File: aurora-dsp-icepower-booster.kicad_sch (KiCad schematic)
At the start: 264 parts, among them J1 24V DC, J10 XLR3_OUT, J11 XLR3_OUT, J12 XLR3_OUT, J13 XLR3_OUT, J14 XLR3_OUT, J2 REMOTE 3.5mm, J3 XLR_IN_1, J4 XLR_IN_2, J5 XLR_IN_3, J6 XLR_IN_4, J7 XLR_IN_5, J8 XLR_IN_6, J9 XLR3_OUT, Q1 BSS138, Q2 BSS138, Q3 BSS138, Q4 BSS138, Q5 BSS138, Q6 BSS138, Q7 BSS138, SW1 ALWAYS/REMOTE, SW2 Gain CH1, SW3 Gain CH2, SW4 Gain CH3, SW5 Gain CH4, SW6 Gain CH5, SW7 Gain CH6, U1 TEL5-2422, U10 LM4562, U11 LM4562, U12 LM4562, U13 LM4562, U14 ADP7118ARDZ-11, U15 ADP7182AUJZ-11, U2 LM4562, U3 LM4562, U4 LM4562, U5 LM4562, U6 LM4562, U7 LM4562, U8 LM4562, U9 LM4562

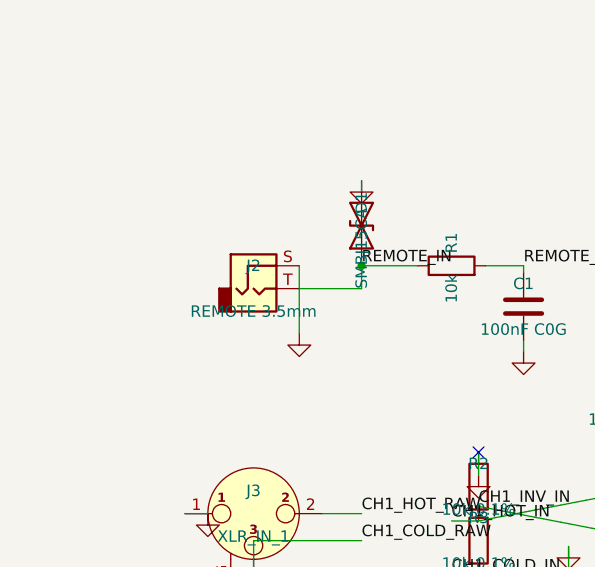
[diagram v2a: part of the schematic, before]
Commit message: feat: Replace J2 Lumberg with KH-PJ-320EA-5P-SMT, add J15 passthrough
- Replaced J2 (Lumberg 1503_02 AudioJack2) with KH-PJ-320EA-5P-SMT (LCSC C5123132)
- Added J15 as identical passthrough jack at (19, 5.08), left of J2 (30.47, 5.08)
- Created custom footprint + symbol with 3D models
- Schematic: J2+J15 Tip→/REMOTE_IN, Sleeve→GND, unused pins→no_connect
- PCB: REMOTE_IN traces routed around J2 Pad5 to avoid short
- DRC: 0 shorts, 0 real unconnected (27 zone fill, 56 warnings)
- ERC: 0 errors, 1059 warnings (baseline)
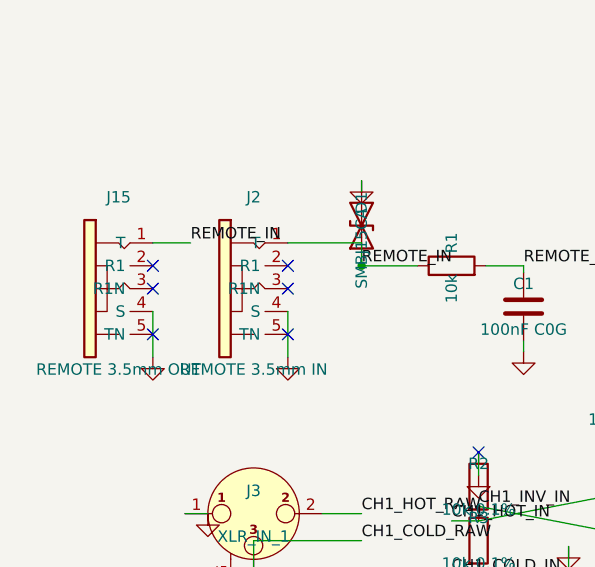
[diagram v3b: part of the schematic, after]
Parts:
- removed J2: REMOTE 3.5mm, Connector_Audio:Jack_3.5mm_Lumberg_1503_02_Horizontal, symbol Connector_Audio:AudioJack2
- added J15: REMOTE 3.5mm OUT, aurora-dsp-icepower-booster:AUDIO-SMD_KH-PJ-320EA-5P-SMT, symbol aurora-dsp-icepower-booster:KH-PJ-320EA-5P-SMT
- added J2: REMOTE 3.5mm IN, aurora-dsp-icepower-booster:AUDIO-SMD_KH-PJ-320EA-5P-SMT, symbol aurora-dsp-icepower-booster:KH-PJ-320EA-5P-SMT
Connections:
- net GND: now also J15.4 (S), J2.4 (S)
- net REMOTE_IN: now also J15.1 (T), J2.1 (T)
- no-connect marks 1 -> 7
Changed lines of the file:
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@@
   (wire (pts (xy 165 178.81) (xy 165 181.35)) (stroke (width 0) (type default)))
   (wire (pts (xy 102.62 552.54) (xy 105 556.19)) (stroke (width 0) (type default)))
-  (wire (pts (xy 42 85) (xy 42 82.46)) (stroke (width 0) (type default)))
   (wire (pts (xy 280 425) (xy 285 425)) (stroke (width 0) (type default)))
   (wire (pts (xy 302 265) (xy 302 266.19)) (stroke (width 0) (type default)))
@@
   (wire (pts (xy 102.62 470) (xy 105 466.19)) (stroke (width 0) (type default)))
   (wire (pts (xy 30 517.62) (xy 30 520)) (stroke (width 0) (type default)))
-  (wire (pts (xy 35.08 82.46) (xy 35.08 90)) (stroke (width 0) (type default)))
   (wire (pts (xy 285 360) (xy 285 361.19)) (stroke (width 0) (type default)))
   (wire (pts (xy 129.84 22.38) (xy 127 22.38)) (stroke (width 0) (type default)))
@@
   (wire (pts (xy 297.62 505) (xy 302 505)) (stroke (width 0) (type default)))
   (wire (pts (xy 242.38 190) (xy 244.92 190)) (stroke (width 0) (type default)))
-  (wire (pts (xy 35.08 85) (xy 42 85)) (stroke (width 0) (type default)))
   (wire (pts (xy 102.62 227.46) (xy 105 216.19)) (stroke (width 0) (type default)))
   (wire (pts (xy 105 563.81) (xy 105 566.35)) (stroke (width 0) (type default)))
@@
       (project "aurora-dsp-icepower-booster"
   (path "/09fde901-d8c0-4b5a-a63a-824cb2cd0bb6" (reference "#PWR046") (unit 1)))))
-  (symbol (lib_id "power:GND") (at 35.08 90 0) (unit 1) (exclude_from_sim no) (in_bom yes) (on_board yes) (dnp no)
-    (property "Reference" "#PWR047" (at 35.08 90 0) (effects (font (size 1.27 1.27)) (hide yes)))
-    (property "Value" "GND" (at 35.08 90 0) (effects (font (size 1.27 1.27)) (hide yes)))
-    (property "Footprint" "" (at 35.08 90 0) (effects (font (size 1.27 1.27)) (hide yes)))
-    (property "Datasheet" "" (at 35.08 90 0) (effects (font (size 1.27 1.27)) (hide yes)))
-    (pin "1")
-    (instances
-      (project "aurora-dsp-icepower-booster"
-  (path "/09fde901-d8c0-4b5a-a63a-824cb2cd0bb6" (reference "#PWR047") (unit 1)))))
   (label "CH5_COLD_RAW" (at 30 440 0) (effects (font (size 1.27 1.27)) (justify left bottom)))
   (label "CH2_EMI_COLD" (at 302 200 0) (effects (font (size 1.27 1.27)) (justify left bottom)))
@@
         (project "aurora-dsp-icepower-booster"
   (path "/09fde901-d8c0-4b5a-a63a-824cb2cd0bb6" (reference "R10") (unit 1)))))
-    (symbol (lib_id "Connector_Audio:AudioJack2") (at 30 85 0) (unit 1) (exclude_from_sim no) (in_bom yes) (on_board yes) (dnp no)
-    (property "Reference" "J2" (at 30 82.46 0) (effects (font (size 1.27 1.27))))
-    (property "Value" "REMOTE 3.5mm" (at 30 87.54 0) (effects (font (size 1.27 1.27))))
-    (property "Footprint" "Connector_Audio:Jack_3.5mm_Lumberg_1503_02_Horizontal" (at 30 85 0) (effects (font (size 1.27 1.27)) (hide yes)))
-    (property "Datasheet" "~" (at 30 85 0) (effects (font (size 1.27 1.27)) (hide yes)))
-    (property "Description" "" (at 30 85 0) (effects (font (size 1.27 1.27))))
-    (pin "S")
-    (pin "T")
-      (instances
-        (project "aurora-dsp-icepower-booster"
-  (path "/09fde901-d8c0-4b5a-a63a-824cb2cd0bb6" (reference "J2") (unit 1)))))
     (symbol (lib_id "Device:R") (at 65 280 0) (unit 1) (exclude_from_sim no) (in_bom yes) (on_board yes) (dnp no)
     (property "Reference" "R16" (at 65 277.46 0) (effects (font (size 1.27 1.27))))
@@
   (wire (pts (xy 285 505) (xy 285 505.19)) (stroke (width 0) (type default)))
   (label "CH6_OUT_COLD" (at 285 506.19 180) (effects (font (size 1.27 1.27)) (justify left bottom)))(label "V+" (at 128.81 27.46 0) (effects (font (size 1.27 1.27)) (justify left bottom)))(label "V-" (at 128.81 70.16 0) (effects (font (size 1.27 1.27)) (justify left bottom)))
+(symbol (lib_id "aurora-dsp-icepower-booster:KH-PJ-320EA-5P-SMT") (at 30 85 0) (unit 1) (exclude_from_sim no) (in_bom yes) (on_board yes) (dnp no)
+    (property "Reference" "J2" (at 30 74.84 0) (effects (font (size 1.27 1.27))))
+    (property "Value" "REMOTE 3.5mm IN" (at 30 93.98 0) (effects (font (size 1.27 1.27))))
+    (property "Footprint" "aurora-dsp-icepower-booster:AUDIO-SMD_KH-PJ-320EA-5P-SMT" (at 30 85 0) (effects (font (size 1.27 1.27)) (hide yes)))
+    (property "Datasheet" "https://www.lcsc.com/datasheet/C5123132.pdf" (at 30 85 0) (effects (font (size 1.27 1.27)) (hide yes)))
+    (property "Description" "3.5mm Stereo Audio Jack SMD 5-Pin with detect switches, Kinghelm, LCSC C5123132" (at 30 85 0) (effects (font (size 1.27 1.27)) (hide yes)))
+    (property "LCSC" "C5123132" (at 30 85 0) (effects (font (size 1.27 1.27)) (hide yes)))
+    (pin "1")
+    (pin "2")
+    (pin "3")
+    (pin "4")
+    (pin "5")
+      (instances
+        (project "aurora-dsp-icepower-booster"
+  (path "/09fde901-d8c0-4b5a-a63a-824cb2cd0bb6" (reference "J2") (unit 1)))))
+(symbol (lib_id "aurora-dsp-icepower-booster:KH-PJ-320EA-5P-SMT") (at 15 85 0) (unit 1) (exclude_from_sim no) (in_bom yes) (on_board yes) (dnp no)
+    (property "Reference" "J15" (at 15 74.84 0) (effects (font (size 1.27 1.27))))
+    (property "Value" "REMOTE 3.5mm OUT" (at 15 93.98 0) (effects (font (size 1.27 1.27))))
+    (property "Footprint" "aurora-dsp-icepower-booster:AUDIO-SMD_KH-PJ-320EA-5P-SMT" (at 15 85 0) (effects (font (size 1.27 1.27)) (hide yes)))
+    (property "Datasheet" "https://www.lcsc.com/datasheet/C5123132.pdf" (at 15 85 0) (effects (font (size 1.27 1.27)) (hide yes)))
+    (property "Description" "3.5mm Stereo Audio Jack SMD 5-Pin with detect switches, Kinghelm, LCSC C5123132" (at 15 85 0) (effects (font (size 1.27 1.27)) (hide yes)))
+    (property "LCSC" "C5123132" (at 15 85 0) (effects (font (size 1.27 1.27)) (hide yes)))
+    (pin "1")
+    (pin "2")
+    (pin "3")
+    (pin "4")
+    (pin "5")
+      (instances
+        (project "aurora-dsp-icepower-booster"
+  (path "/09fde901-d8c0-4b5a-a63a-824cb2cd0bb6" (reference "J15") (unit 1)))))
+(symbol (lib_id "power:GND") (at 33.81 92.62 0) (unit 1) (exclude_from_sim no) (in_bom yes) (on_board yes) (dnp no)
+    (property "Reference" "#PWR0154" (at 33.81 92.62 0) (effects (font (size 1.27 1.27)) (hide yes)))
+    (property "Value" "GND" (at 33.81 92.62 0) (effects (font (size 1.27 1.27)) (hide yes)))
+    (property "Footprint" "" (at 33.81 92.62 0) (effects (font (size 1.27 1.27)) (hide yes)))
+    (property "Datasheet" "" (at 33.81 92.62 0) (effects (font (size 1.27 1.27)) (hide yes)))
+    (pin "1")
+    (instances
+      (project "aurora-dsp-icepower-booster"
+  (path "/09fde901-d8c0-4b5a-a63a-824cb2cd0bb6" (reference "#PWR0154") (unit 1)))))
+(symbol (lib_id "power:GND") (at 18.81 92.62 0) (unit 1) (exclude_from_sim no) (in_bom yes) (on_board yes) (dnp no)
+    (property "Reference" "#PWR0155" (at 18.81 92.62 0) (effects (font (size 1.27 1.27)) (hide yes)))
+    (property "Value" "GND" (at 18.81 92.62 0) (effects (font (size 1.27 1.27)) (hide yes)))
+    (property "Footprint" "" (at 18.81 92.62 0) (effects (font (size 1.27 1.27)) (hide yes)))
+    (property "Datasheet" "" (at 18.81 92.62 0) (effects (font (size 1.27 1.27)) (hide yes)))
+    (pin "1")
+    (instances
+      (project "aurora-dsp-icepower-booster"
+  (path "/09fde901-d8c0-4b5a-a63a-824cb2cd0bb6" (reference "#PWR0155") (unit 1)))))
+  (wire (pts (xy 33.81 79.92) (xy 42 79.92)) (stroke (width 0) (type default)))
+  (wire (pts (xy 42 79.92) (xy 42 82.46)) (stroke (width 0) (type default)))
+  (wire (pts (xy 33.81 87.54) (xy 33.81 92.62)) (stroke (width 0) (type default)))
+  (wire (pts (xy 18.81 79.92) (xy 23 79.92)) (stroke (width 0) (type default)))
+  (wire (pts (xy 18.81 87.54) (xy 18.81 92.62)) (stroke (width 0) (type default)))
+  (no_connect (at 33.81 82.46))
+  (no_connect (at 33.81 85))
+  (no_connect (at 33.81 90.08))
+  (no_connect (at 18.81 82.46))
+  (no_connect (at 18.81 85))
+  (no_connect (at 18.81 90.08))
+  (label "REMOTE_IN" (at 23 79.92 0) (effects (font (size 1.27 1.27)) (justify left bottom)))
 )

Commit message: refactor: Projekt standalone gemacht + bereinigt
Standalone:
- 17 System-Footprints (.kicad_mod) in footprints.pretty/ kopiert
- 15 System-3D-Modelle (.step) in footprints.pretty/3dshapes/ kopiert
- Alle 3D-Pfade in PCB von ${KICAD9_3DMODEL_DIR} auf ${KIPRJMOD} umgeschrieben (249 Referenzen)
- Alle Schaltplan-Footprint-Refs von System-Libraries auf project: umgeschrieben (287 Referenzen)
- sym-lib-table: Absoluten Pfad durch ${KIPRJMOD} ersetzt
- Projekt läuft ohne KiCad-Systemlibraries

Bereinigt:
- 70 Dateien gelöscht (Einmal-Analyse-Skripte, alte Reports, Duplikate)
- 2 Verzeichnisse entfernt (footprints/, aurora-dsp-icepower-booster-backups/)
- Alte/unbenutzte 3D-Modelle entfernt (Lumberg, NC3MBH Duplikat)
- .gitignore erweitert (*.rpt, *.net)
- scripts/: Von ~65 auf 20 reduziert (nur Kern-Workflows behalten)

Verifikation:
- DRC: 709 violations, 27 unconnected (keine Regression)
- ERC: 1067 violations (unverändert)
- 21 Footprints, 19 3D-Modelle — alle lokal vorhanden
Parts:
- C1, C10, C11, C12, C13, C14, C15, C18, C19, C2, C22, C23, C24, C25, C26, C27, C28, C29, C3, C30, C31, C32, C33, C34, C35, C36, C37, C38, C39, C4, C40, C41, C42, C43, C44, C45, C46, C47, C48, C49, C5, C50, C51, C52, C53, C54, C55, C56, C57, C58, C59, C6, C60, C61, C7, C74, C75, C76, C77, C78, C79, C8, C80, C9: footprint Capacitor_SMD:C_0805_2012Metric -> project:C_0805_2012Metric
- C16, C17, C20, C21: footprint Capacitor_SMD:C_1210_3225Metric -> project:C_1210_3225Metric
- C62, C63, C64, C65, C66, C67, C68, C69, C70, C71, C72, C73: footprint Capacitor_SMD:C_1206_3216Metric -> project:C_1206_3216Metric
- C81: footprint Capacitor_SMD:C_0402_1005Metric -> project:C_0402_1005Metric
- D1: footprint Diode_SMD:D_SMB -> project:D_SMB
- D10, D11, D12, D13, D14, D15, D16, D17, D18, D19, D2, D20, D21, D22, D23, D24, D25, D3, D4, D5, D6, D7, D8, D9: footprint Diode_SMD:D_SOD-323 -> project:D_SOD-323
- FB1, FB2: footprint Inductor_SMD:L_0805_2012Metric -> project:L_0805_2012Metric
- J1: footprint Connector_BarrelJack:BarrelJack_Horizontal -> project:BarrelJack_Horizontal
- J10, J11, J12, J13, J14, J9: footprint Connector_Audio:Jack_XLR_Neutrik_NC3MBH_Horizontal -> project:Jack_XLR_Neutrik_NC3MBH_Horizontal
- J3, J4, J5, J6, J7, J8: footprint Connector_Audio:Jack_XLR_Neutrik_NC3FBH2_Horizontal -> project:Jack_XLR_Neutrik_NC3FBH2_Horizontal
- Q1, Q2, Q3, Q4, Q5, Q6, Q7: footprint Package_TO_SOT_SMD:SOT-23 -> project:SOT-23
- R1, R10, R100, R101, R102, R103, R104, R105, R106, R107, R108, R109, R11, R110, R111, R112, R113, R12, R13, R14, R15, R16, R17, R18, R19, R2, R20, R21, R22, R23, R24, R25, R26, R27, R28, R29, R3, R30, R31, R32, R33, R34, R35, R36, R37, R38, R39, R4, R40, R41, R42, R43, R44, R45, R46, R47, R48, R49, R5, R50, R51, R52, R53, R54, R55, R56, R57, R58, R59, R6, R60, R61, R62, R63, R64, R65, R66, R67, R68, R69, R7, R70, R71, R72, R73, R74, R75, R76, R77, R78, R79, R8, R80, R81, R82, R83, R84, R85, R86, R87, R88, R89, R9, R90, R91, R92, R93, R94, R95, R96, R97, R98, R99: footprint Resistor_SMD:R_0805_2012Metric -> project:R_0805_2012Metric
- SW1: footprint Button_Switch_THT:SW_E-Switch_EG1224_SPDT_Angled -> project:SW_E-Switch_EG1224_SPDT_Angled
- SW2, SW3, SW4, SW5, SW6, SW7: footprint Button_Switch_SMD:SW_DIP_SPSTx03_Slide_Omron_A6S-310x_W8.9mm_P2.54mm -> project:SW_DIP_SPSTx03_Slide_Omron_A6S-310x_W8.9mm_P2.54mm
- U10, U11, U12, U13, U2, U3, U4, U5, U6, U7, U8, U9: footprint Package_SO:SOIC-8_3.9x4.9mm_P1.27mm -> project:SOIC-8_3.9x4.9mm_P1.27mm
- U15: footprint Package_TO_SOT_SMD:SOT-23-5 -> project:SOT-23-5
